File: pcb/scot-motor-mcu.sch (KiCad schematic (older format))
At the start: 51 parts, among them IC2 STM32F0xxKxTx, IC3 NCV8450A, J8 Conn_01x03_Male, P1 SWD, Q1 BC817, U1 LTV-357T, U10 74AHC1G08, U2 74HC00, U3 LTV-357T, U4 LTV-357T, U5 DRV8872DDA, Y1 Crystal_GND24

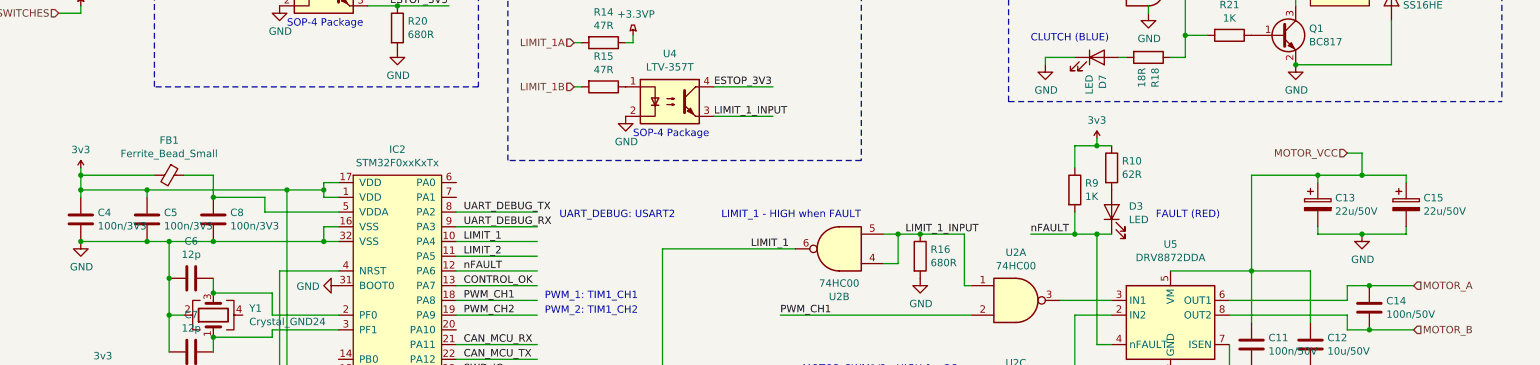
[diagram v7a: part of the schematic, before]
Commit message: pcb: Add BOM list. Adjust some values to reduce lines.
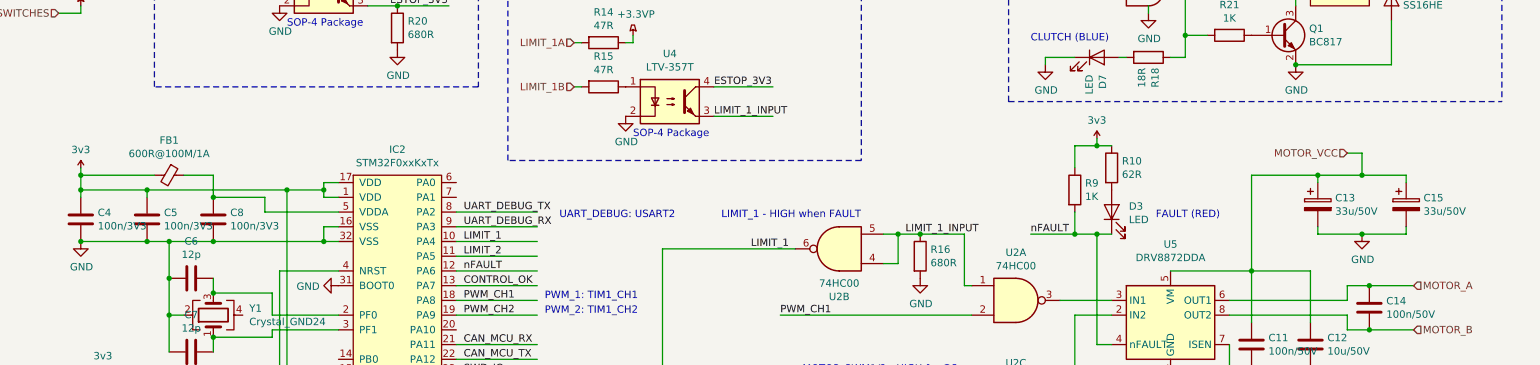
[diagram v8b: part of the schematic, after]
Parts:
- C13, C15: value 22u/50V -> 33u/50V
- FB1: value Ferrite_Bead_Small -> 600R@100M/1A
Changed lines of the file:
@@
 P 9900 3050
 F 0 "C13" H 10018 3096 50  0000 L CNN
-F 1 "22u/50V" H 10018 3005 50  0000 L CNN
+F 1 "33u/50V" H 10018 3005 50  0000 L CNN
 F 2 "Capacitor_SMD:CP_Elec_8x10.5" H 9938 2900 50  0001 C CNN
 F 3 "~" H 9900 3050 50  0001 C CNN
@@
 P 10500 3050
 F 0 "C15" H 10618 3096 50  0000 L CNN
-F 1 "22u/50V" H 10618 3005 50  0000 L CNN
+F 1 "33u/50V" H 10618 3005 50  0000 L CNN
 F 2 "Capacitor_SMD:CP_Elec_8x10.5" H 10538 2900 50  0001 C CNN
 F 3 "~" H 10500 3050 50  0001 C CNN
@@
 P 2100 2850
 F 0 "FB1" V 1863 2850 50  0000 C CNN
-F 1 "Ferrite_Bead_Small" V 1954 2850 50  0000 C CNN
+F 1 "600R@100M/1A" V 1954 2850 50  0000 C CNN
 F 2 "Inductor_SMD:L_0805_2012Metric_Pad1.15x1.40mm_HandSolder" V 2030 2850 50  0001 C CNN
 F 3 "~" H 2100 2850 50  0001 C CNN
